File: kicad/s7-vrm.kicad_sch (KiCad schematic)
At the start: 31 parts, among them J1 Conn_02x15_Row_Letter_First, Q1 Q_NPN_BEC, Q2 Q_NMOS_GDS, Q3 Q_NMOS_GDS, SW1 SW_DIP_x04, U1 NCP1579

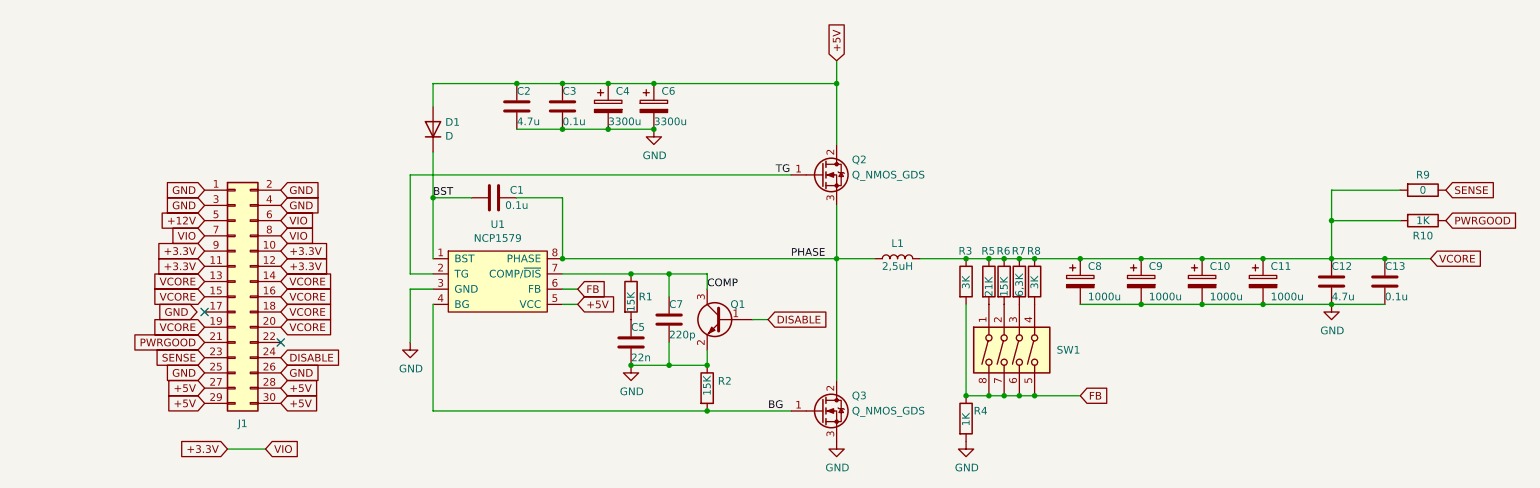
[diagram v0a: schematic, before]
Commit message: Revision 0.4
- Added optional 1uF capacitors on input and output
- Increased the size of the inductor pins for SMD option
- Minor layout fixes
- Updated silk layer, logos etc.
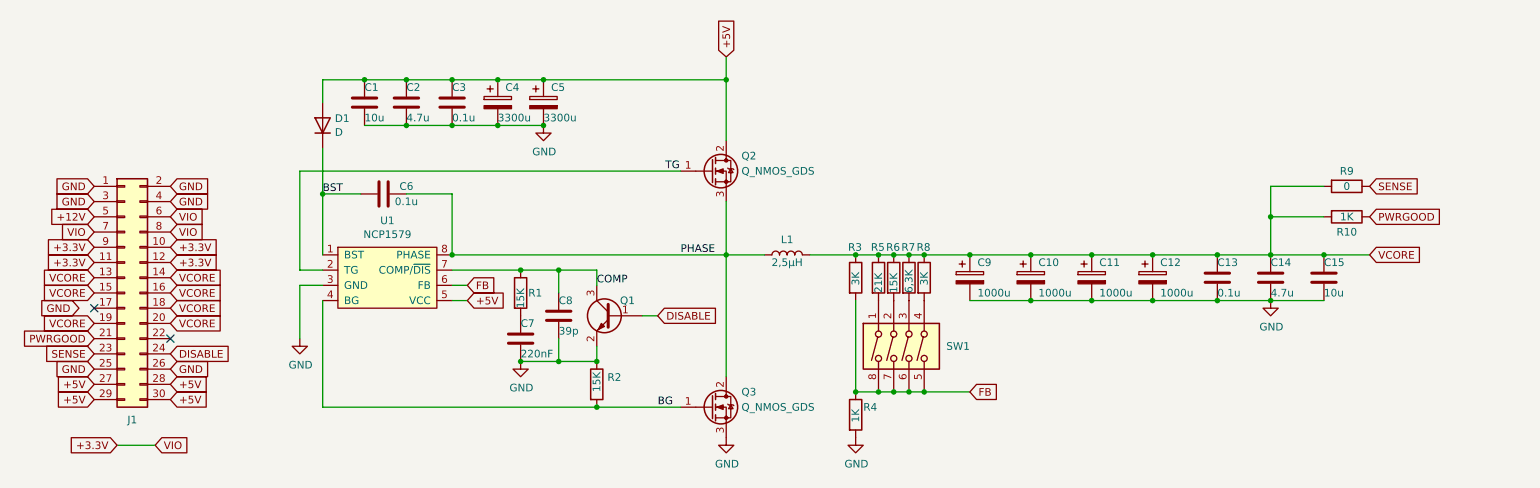
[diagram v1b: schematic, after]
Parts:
- added C1, C15: 10u, Capacitor_SMD:C_1206_3216Metric_Pad1.33x1.80mm_HandSolder, symbol Device:C
- C7: renamed from C5; value 22n -> 220nF; LCSC C282848 -> C107186
- C8: renamed from C7; value 220p -> 39p; LCSC C377077 -> C541493
- L1: value 2,5uH -> 2,5µH; footprint Inductor_THT:L_Toroid_Vertical_L16.0mm_W8.0mm_P7.62mm -> Inductor_THT:L_Toroid_Horizontal_D6.5mm_P10.00mm_Diameter7-5mm_Amidon-T25
- R1: LCSC C229767 -> C144515
- renumbered C9 to C10, C10 to C11, C11 to C12, C12 to C14, C6 to C5, C1 to C6, C8 to C9
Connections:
- net +5V: now also C1.1
- net GND: now also C1.2, C15.2
- net VCORE: now also C15.1
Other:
- title: MMX-VRM -> S7-VRM
- moved on the sheet: C10, C11, C12, C13, C14, C2, C3, C4, C5, C6, C7, C8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

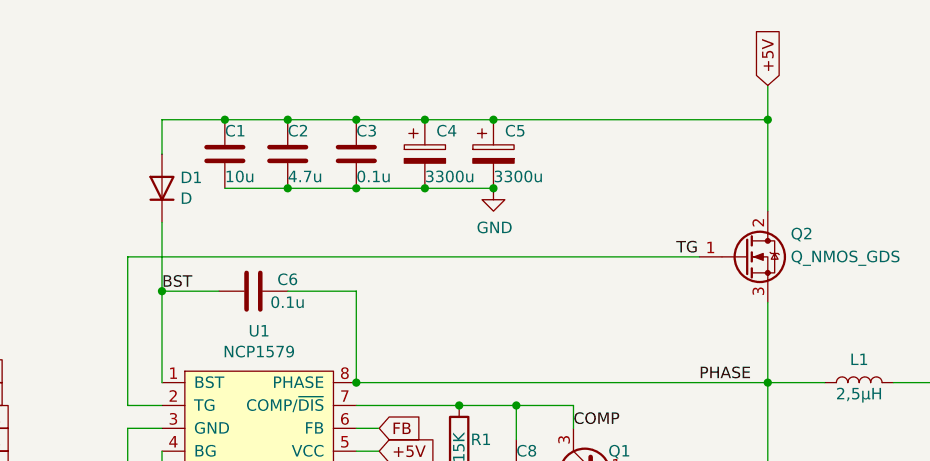
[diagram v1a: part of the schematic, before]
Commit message: Updated documentation and part numbers
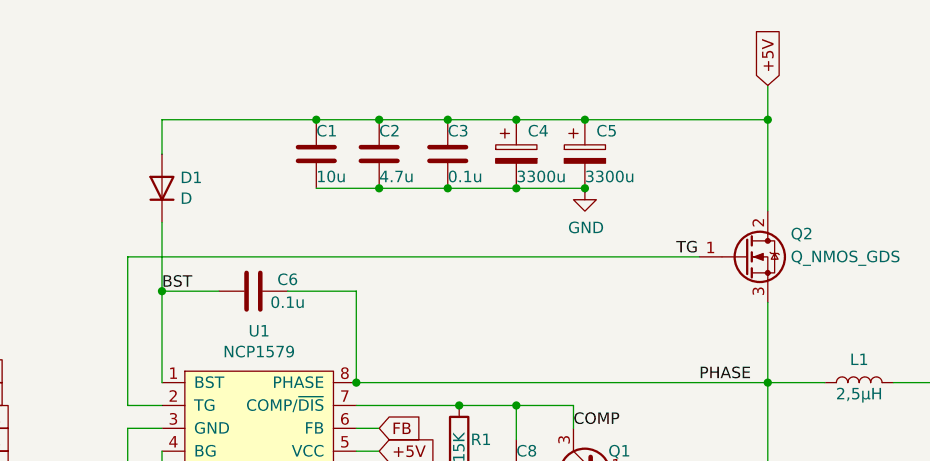
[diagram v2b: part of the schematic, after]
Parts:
- C14, C2: LCSC C105997 -> C51205
- L1: LCSC (none) -> C230667
- R5: LCSC C229446 -> C3000607
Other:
- moved on the sheet: C1, C2, C3, C4, C5

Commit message: Layout improvements
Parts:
- renumbered R4 to R3, R3 to R4
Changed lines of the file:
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@@
   (title_block
     (title "S7-VRM")
-    (date "2023-04-01")
+    (date "2023-04-03")
     (rev "0.4")
     (company "Necroware")
@@
   (symbol (lib_id "Device:R") (at 172.085 123.825 0) (unit 1)
     (in_bom yes) (on_board yes) (dnp no)
-    (property "Reference" "R4" (at 173.355 122.555 0)
+    (property "Reference" "R3" (at 173.355 122.555 0)
       (effects (font (size 1.27 1.27)) (justify left))
     )
@@
     )
     (property "LCSC" "C144508" (at 172.085 123.825 0)
+      (effects (font (size 1.27 1.27)) hide)
+    )
+    (pin "1")
+    (pin "2")
+    (instances
+      (project "s7-vrm"
+        (path "/30f15357-ce1d-48b9-93dc-7d9b1b2aa048"
+          (reference "R3") (unit 1)
+        )
+      )
+    )
+  )
+  (symbol (lib_id "Device:R") (at 172.085 100.965 0) (unit 1)
+    (in_bom yes) (on_board yes) (dnp no)
+    (property "Reference" "R4" (at 170.815 95.885 0)
+      (effects (font (size 1.27 1.27)) (justify left))
+    )
+    (property "Value" "3K" (at 172.085 102.235 90)
+      (effects (font (size 1.27 1.27)) (justify left))
+    )
+    (property "Footprint" "Resistor_SMD:R_1206_3216Metric_Pad1.30x1.75mm_HandSolder" (at 170.307 100.965 90)
+      (effects (font (size 1.27 1.27)) hide)
+    )
+    (property "Datasheet" "~" (at 172.085 100.965 0)
+      (effects (font (size 1.27 1.27)) hide)
+    )
+    (property "LCSC" "C229609" (at 172.085 100.965 0)
       (effects (font (size 1.27 1.27)) hide)
     )
@@
         )
       )
-    )
-  )
-  (symbol (lib_id "Device:R") (at 172.085 100.965 0) (unit 1)
-    (in_bom yes) (on_board yes) (dnp no)
-    (property "Reference" "R3" (at 170.815 95.885 0)
-      (effects (font (size 1.27 1.27)) (justify left))
-    )
-    (property "Value" "3K" (at 172.085 102.235 90)
-      (effects (font (size 1.27 1.27)) (justify left))
-    )
-    (property "Footprint" "Resistor_SMD:R_1206_3216Metric_Pad1.30x1.75mm_HandSolder" (at 170.307 100.965 90)
-      (effects (font (size 1.27 1.27)) hide)
-    )
-    (property "Datasheet" "~" (at 172.085 100.965 0)
-      (effects (font (size 1.27 1.27)) hide)
-    )
-    (property "LCSC" "C229609" (at 172.085 100.965 0)
-      (effects (font (size 1.27 1.27)) hide)
-    )
-    (pin "1")
-    (pin "2")
-    (instances
-      (project "s7-vrm"
-        (path "/30f15357-ce1d-48b9-93dc-7d9b1b2aa048"
-          (reference "R3") (unit 1)
-        )
-      )

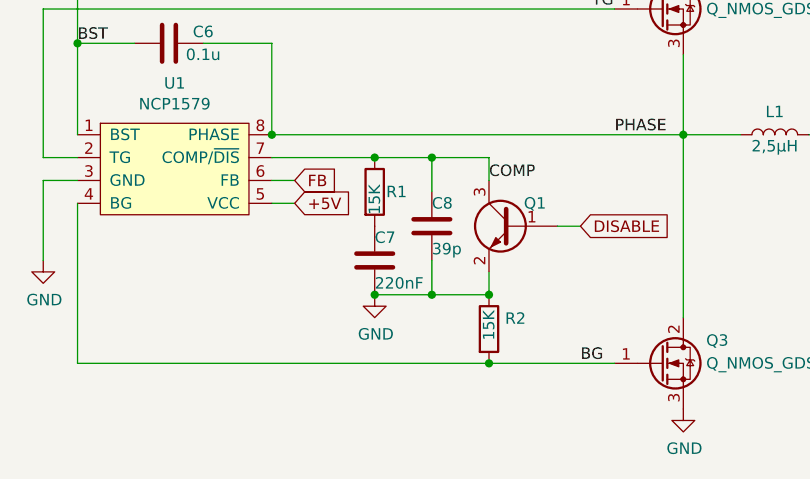
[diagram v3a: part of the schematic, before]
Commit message: Fixed BOM in readme, fixed part numbers in schematics
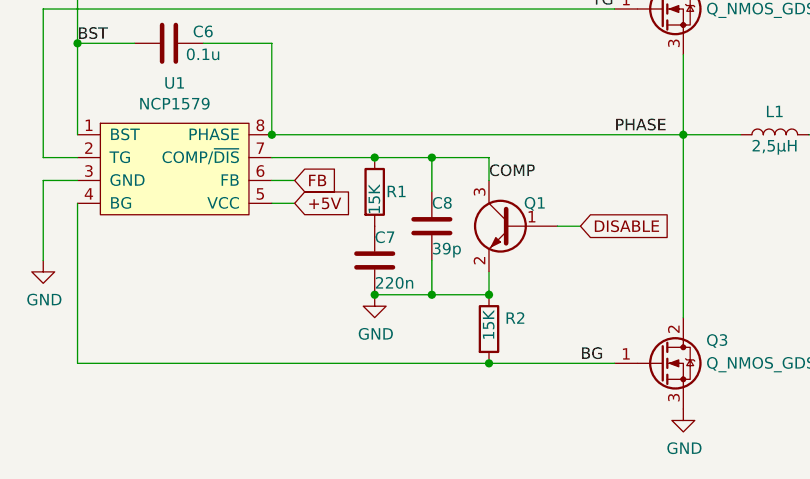
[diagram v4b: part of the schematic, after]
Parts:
- C7: value 220nF -> 220n
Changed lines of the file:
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@@
       (effects (font (size 1.27 1.27)) (justify left))
     )
-    (property "Value" "220nF" (at 116.205 113.665 0)
+    (property "Value" "220n" (at 116.205 113.665 0)
       (effects (font (size 1.27 1.27)) (justify left))
     )

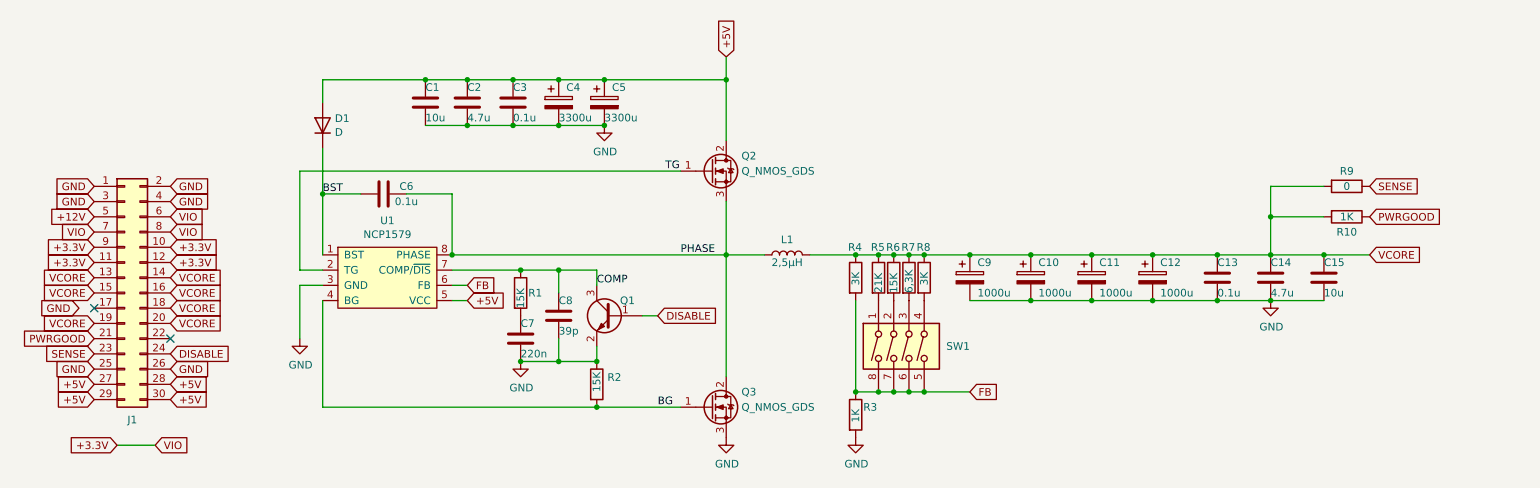
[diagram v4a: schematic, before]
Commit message: Update parts numbers
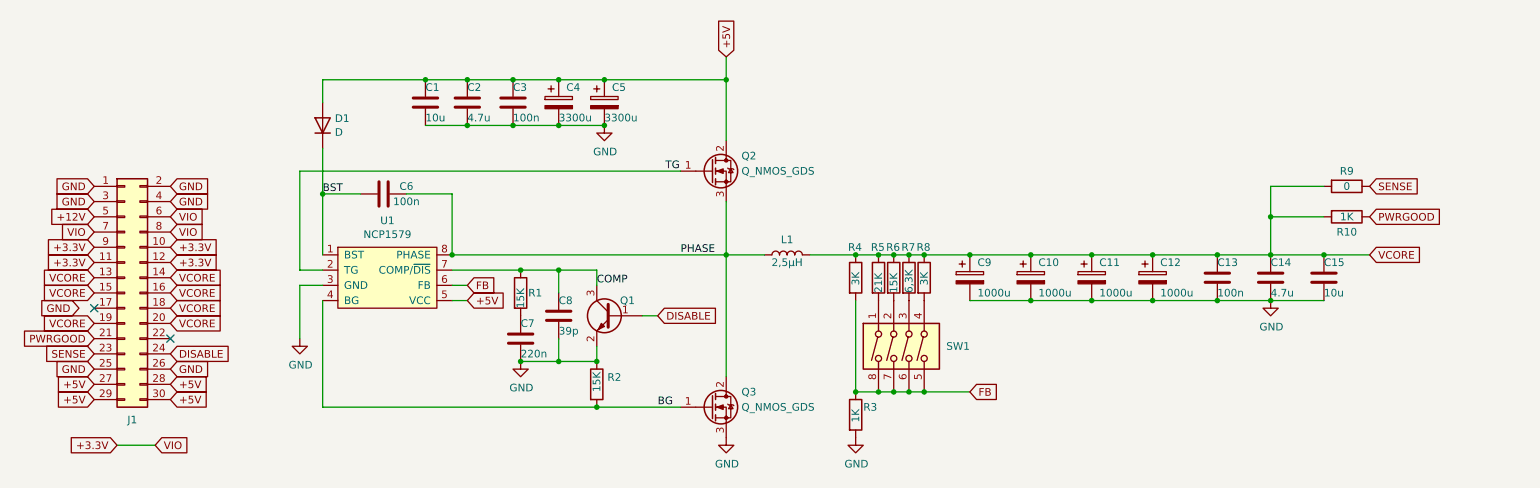
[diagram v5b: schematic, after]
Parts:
- C13, C3, C6: value 0.1u -> 100n
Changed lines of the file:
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@@
       (effects (font (size 1.27 1.27)))
     )
-    (property "Value" "0.1u" (at 97.155 88.265 90)
+    (property "Value" "100n" (at 97.155 88.265 90)
       (effects (font (size 1.27 1.27)))
     )
@@
       (effects (font (size 1.27 1.27)) (justify left))
     )
-    (property "Value" "0.1u" (at 114.935 74.295 0)
+    (property "Value" "100n" (at 114.935 74.295 0)
       (effects (font (size 1.27 1.27)) (justify left))
     )
@@
       (effects (font (size 1.27 1.27)) (justify left))
     )
-    (property "Value" "0.1u" (at 232.41 103.505 0)
-      (effects (font (size 1.27 1.27)) (justify left))
-    )
+    (property "Value" "100n" (at 232.41 103.505 0)
+      (effects (font (size 1.27 1.27)) (justify left))
+    )

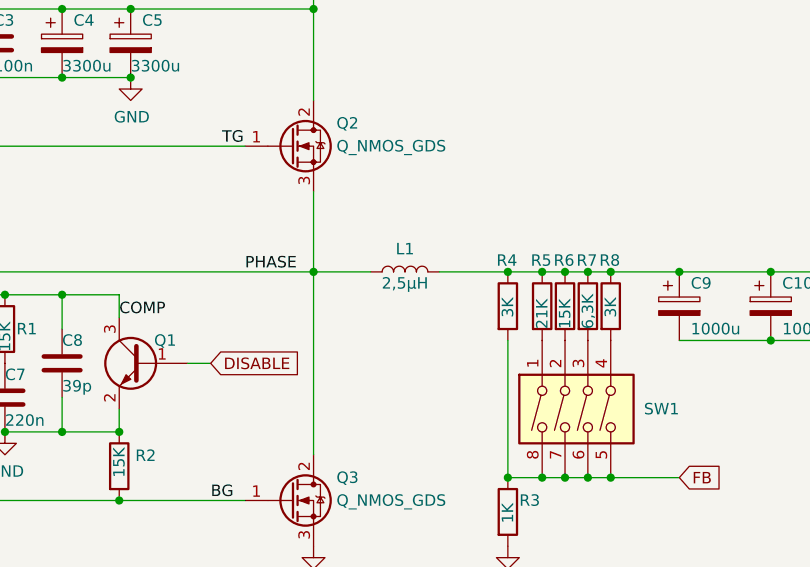
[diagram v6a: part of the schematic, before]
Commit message: Updated parts and documenttion
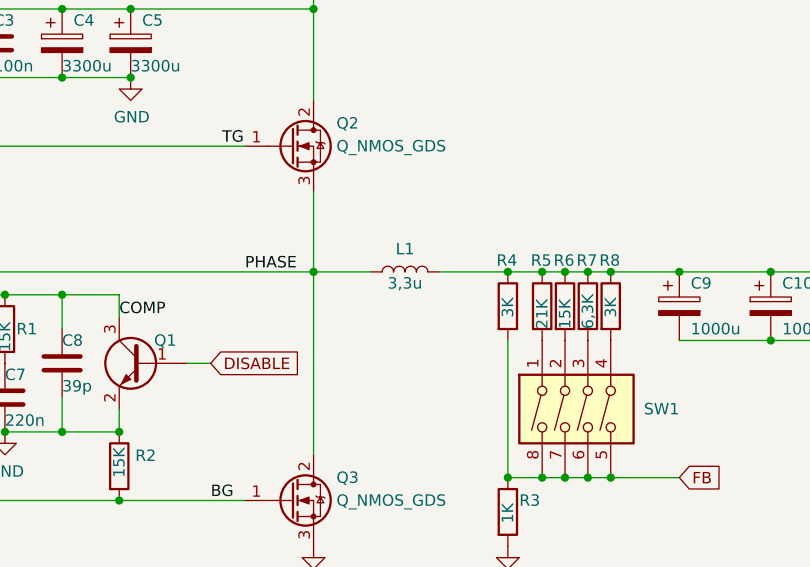
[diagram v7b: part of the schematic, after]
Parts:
- L1: value 2,5µH -> 3,3u; footprint Inductor_THT:L_Toroid_Horizontal_D6.5mm_P10.00mm_Diameter7-5mm_Amidon-T25 -> Inductor_THT:L_Toroid_Vertical_L16.0mm_W8.0mm_P7.62mm; LCSC C230667 -> (none)
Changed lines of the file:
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@@
       (effects (font (size 1.27 1.27)))
     )
-    (property "Value" "2,5µH" (at 160.655 98.425 90)
+    (property "Value" "3,3u" (at 160.655 98.425 90)
       (effects (font (size 1.27 1.27)))
     )
-    (property "Footprint" "Inductor_THT:L_Toroid_Horizontal_D6.5mm_P10.00mm_Diameter7-5mm_Amidon-T25" (at 160.655 97.155 0)
+    (property "Footprint" "Inductor_THT:L_Toroid_Vertical_L16.0mm_W8.0mm_P7.62mm" (at 160.655 97.155 0)
       (effects (font (size 1.27 1.27)) hide)
     )
@@
       (effects (font (size 1.27 1.27)) hide)
     )
-    (property "LCSC" "C230667" (at 160.655 97.155 0)
+    (property "LCSC" "" (at 160.655 97.155 0)
       (effects (font (size 1.27 1.27)) hide)
     )

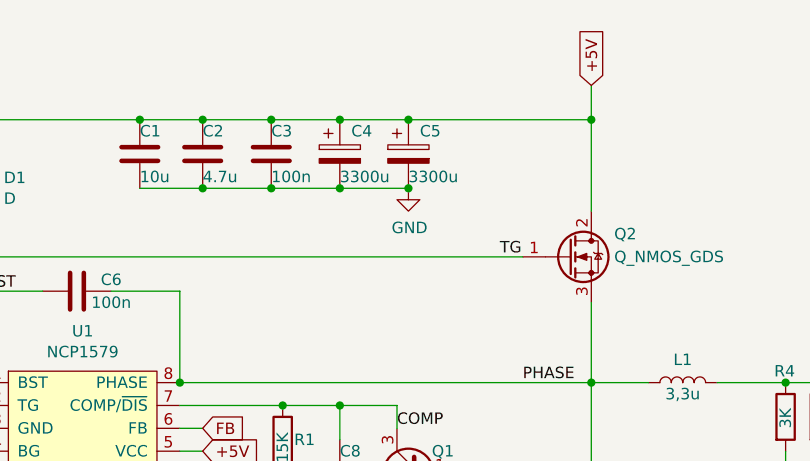
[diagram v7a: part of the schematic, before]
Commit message: Take shorter input capacitor
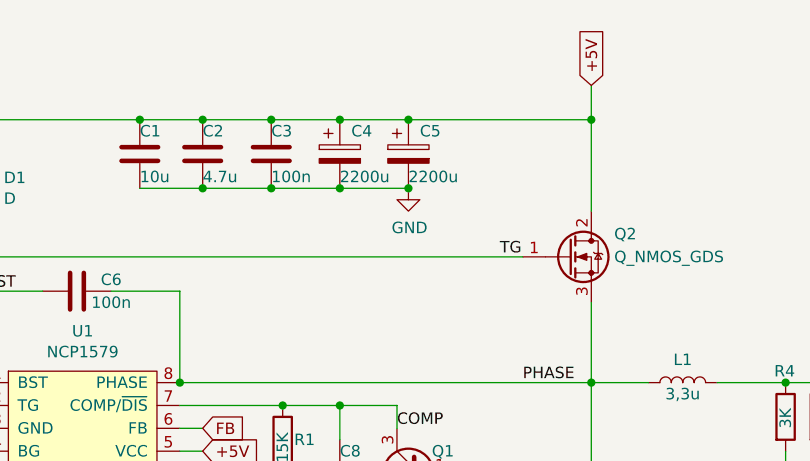
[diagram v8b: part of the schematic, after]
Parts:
- C4, C5: value 3300u -> 2200u; LCSC C407862 -> C407963
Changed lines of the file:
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@@
       (effects (font (size 1.27 1.27)) (justify left))
     )
-    (property "Value" "3300u" (at 122.555 74.295 0)
+    (property "Value" "2200u" (at 122.555 74.295 0)
       (effects (font (size 1.27 1.27)) (justify left))
     )
@@
       (effects (font (size 1.27 1.27)) hide)
     )
-    (property "LCSC" "C407862" (at 122.555 71.755 0)
+    (property "LCSC" "C407963" (at 122.555 71.755 0)
       (effects (font (size 1.27 1.27)) hide)
     )
@@
       (effects (font (size 1.27 1.27)) (justify left))
     )
-    (property "Value" "3300u" (at 130.175 74.295 0)
+    (property "Value" "2200u" (at 130.175 74.295 0)
       (effects (font (size 1.27 1.27)) (justify left))
     )
@@
       (effects (font (size 1.27 1.27)) hide)
     )
-    (property "LCSC" "C407862" (at 130.175 71.755 0)
+    (property "LCSC" "C407963" (at 130.175 71.755 0)
       (effects (font (size 1.27 1.27)) hide)
     )
